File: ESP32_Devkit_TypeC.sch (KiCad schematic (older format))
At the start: 43 parts, among them J1 USB_C_Receptacle_USB2.0, J2 Conn_01x19, J3 Conn_01x19, Q1 SS8050, Q2 SS8050, SW1 EN, SW2 BOOT, U1 MP2451, U2 CH340G, U3 ESP32-PICO-D4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

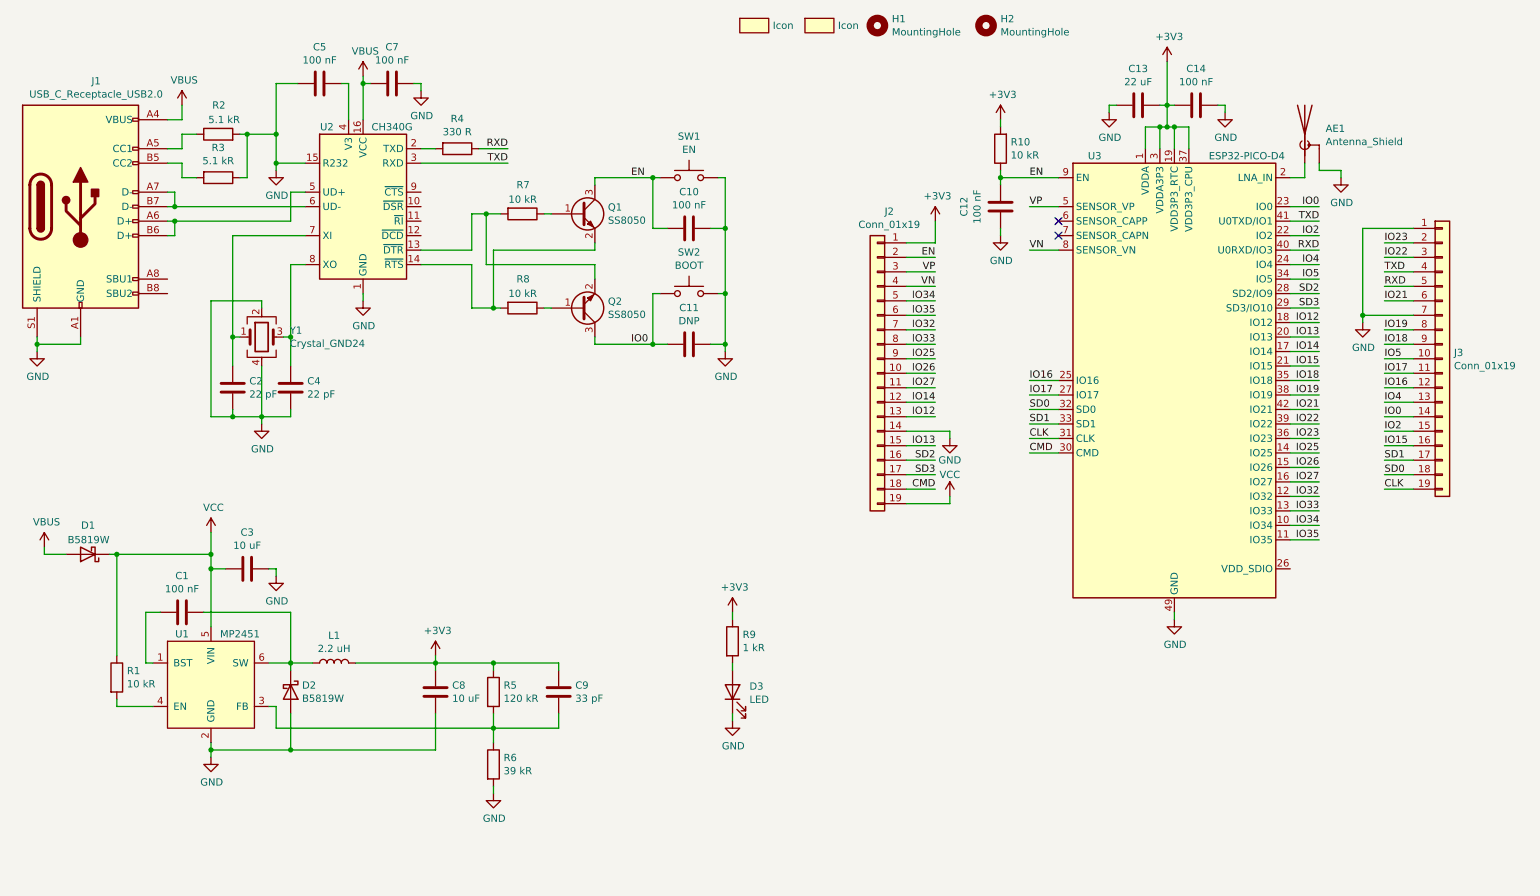
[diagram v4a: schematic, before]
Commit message: Rev B
Changes from Rev A:
 - Fix ESP32 Pico D4 footprint, now LGA
 - Add couple capacitor from EN to IO0
 - Add protection resistors to EN and IO0
 - Move VBUS diode for easier USB Type C jack assembly
 - Small routing optimizations
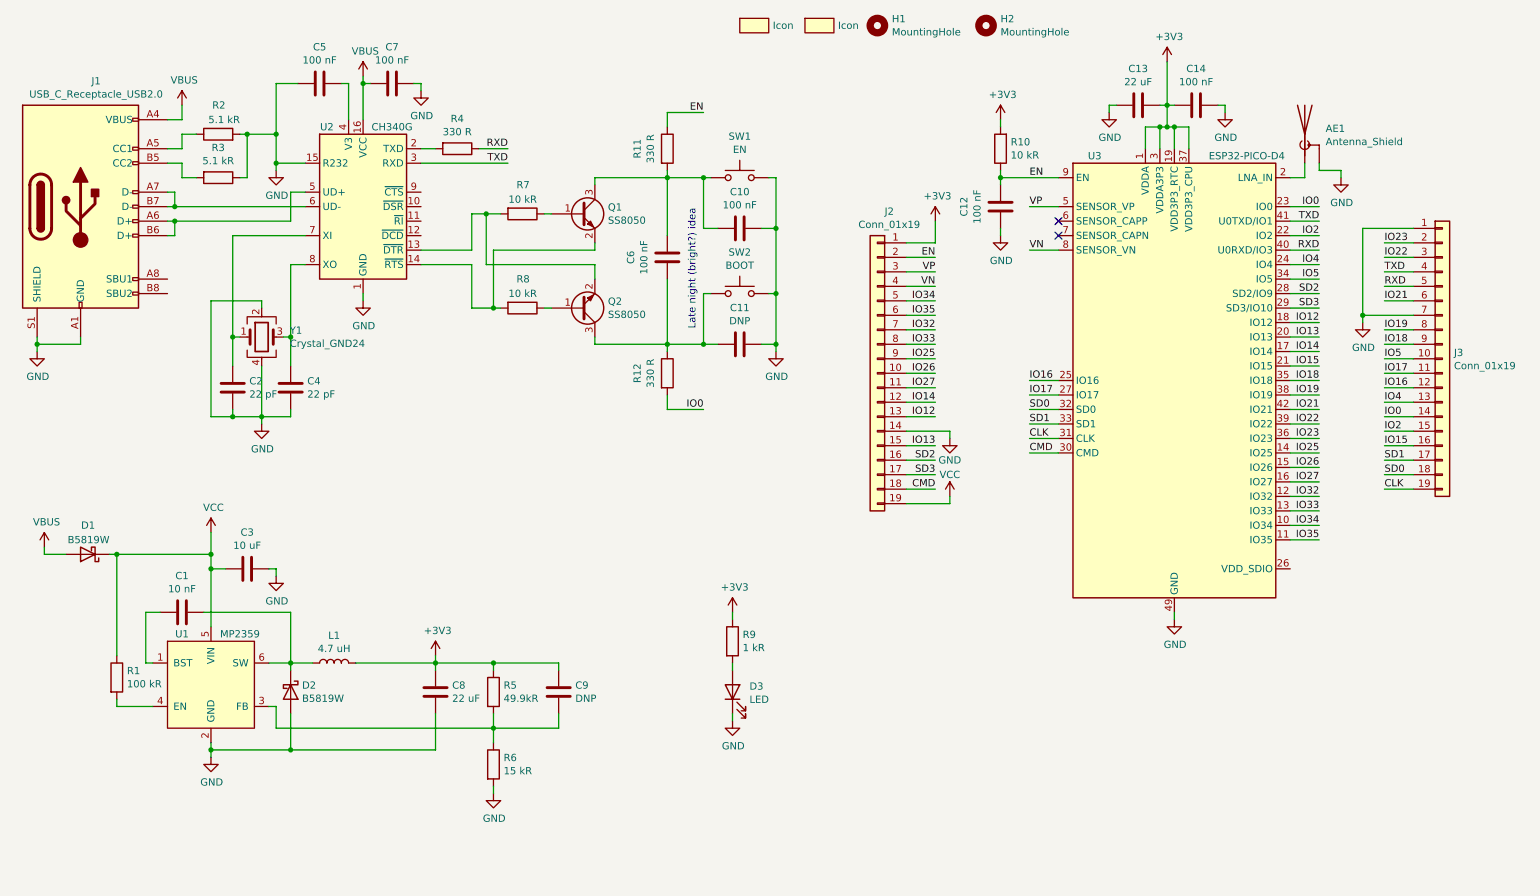
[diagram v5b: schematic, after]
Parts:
- added C6: 100 nF, Capacitor_SMD:C_0402_1005Metric, symbol Device:C
- added R11, R12: 330 R, Resistor_SMD:R_0402_1005Metric, symbol Device:R
- C1: value 100 nF -> 10 nF; LCSC C1525 -> C15195
- C8: value 10 uF -> 22 uF; LCSC C19702 -> C59461
- C9: value 33 pF -> DNP; LCSC C1562 -> (none)
- L1: value 2.2 uH -> 4.7 uH; LCSC C86074 -> C86070
- R1: value 10 kR -> 100 kR; LCSC C25744 -> C25741
- R5: value 120 kR -> 49.9kR; LCSC C25750 -> C25897
- R6: value 39 kR -> 15 kR; LCSC C25783 -> C25756
- U1: value MP2451 -> MP2359; LCSC C14123 -> C14259
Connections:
- net EN: now also R11.1; no longer C10.2, Q1.3 (C), SW1.1
- net IO0: now also R12.2; no longer C11.2, Q2.3 (C), SW2.1
- new net: C10.2, C6.1, Q1.3 (C), R11.2, SW1.1
- new net: C11.2, C6.2, Q2.3 (C), R12.1, SW2.1
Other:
- note added: "Late night (bright?) idea"
- moved on the sheet: C10, C11, SW1, SW2
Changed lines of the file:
@@
 P 2200 5150
 F 0 "U1" H 2000 5500 50  0000 C CNN
-F 1 "MP2451" H 2400 5500 50  0000 C CNN
+F 1 "MP2359" H 2400 5500 50  0000 C CNN
 F 2 "Package_TO_SOT_SMD:SOT-23-6" H 2200 6100 50  0001 C CNN
 F 3 "https://datasheet.lcsc.com/szlcsc/Monolithic-Power-Systems-MPS-MP2451DT-LF-Z_C14123.pdf" H 2200 6100 50  0001 C CNN
-F 4 "C14123" H 2200 5150 50  0001 C CNN "LCSC"
+F 4 "C14259" H 2200 5150 50  0001 C CNN "LCSC"
 	1    2200 5150
 	1    0    0    -1
@@
 P 3050 5000
 F 0 "L1" V 3240 5000 50  0000 C CNN
-F 1 "2.2 uH" V 3149 5000 50  0000 C CNN
+F 1 "4.7 uH" V 3149 5000 50  0000 C CNN
 F 2 "Inductor_SMD:L_1210_3225Metric" H 3050 5000 50  0001 C CNN
 F 3 "~" H 3050 5000 50  0001 C CNN
-F 4 "C86074" V 3050 5000 50  0001 C CNN "LCSC"
+F 4 "C86070" V 3050 5000 50  0001 C CNN "LCSC"
 	1    3050 5000
 	0    -1   -1   0
@@
 P 3750 5200
 F 0 "C8" H 3865 5246 50  0000 L CNN
-F 1 "10 uF" H 3865 5155 50  0000 L CNN
+F 1 "22 uF" H 3865 5155 50  0000 L CNN
 F 2 "Capacitor_SMD:C_0603_1608Metric" H 3788 5050 50  0001 C CNN
 F 3 "~" H 3750 5200 50  0001 C CNN
-F 4 "C19702" H 3750 5200 50  0001 C CNN "LCSC"
+F 4 "C59461" H 3750 5200 50  0001 C CNN "LCSC"
 	1    3750 5200
 	1    0    0    -1
@@
 P 4150 5200
 F 0 "R5" H 4220 5246 50  0000 L CNN
-F 1 "120 kR" H 4220 5155 50  0000 L CNN
+F 1 "49.9kR" H 4220 5155 50  0000 L CNN
 F 2 "Resistor_SMD:R_0402_1005Metric" V 4080 5200 50  0001 C CNN
 F 3 "~" H 4150 5200 50  0001 C CNN
-F 4 "C25750" H 4150 5200 50  0001 C CNN "LCSC"
+F 4 "C25897" H 4150 5200 50  0001 C CNN "LCSC"
 	1    4150 5200
 	1    0    0    -1
@@
 P 4150 5700
 F 0 "R6" H 4220 5746 50  0000 L CNN
-F 1 "39 kR" H 4220 5655 50  0000 L CNN
+F 1 "15 kR" H 4220 5655 50  0000 L CNN
 F 2 "Resistor_SMD:R_0402_1005Metric" V 4080 5700 50  0001 C CNN
 F 3 "~" H 4150 5700 50  0001 C CNN
-F 4 "C25783" H 4150 5700 50  0001 C CNN "LCSC"
+F 4 "C25756" H 4150 5700 50  0001 C CNN "LCSC"
 	1    4150 5700
 	1    0    0    -1
@@
 P 4600 5200
 F 0 "C9" H 4715 5246 50  0000 L CNN
-F 1 "33 pF" H 4715 5155 50  0000 L CNN
+F 1 "DNP" H 4715 5155 50  0000 L CNN
 F 2 "Capacitor_SMD:C_0402_1005Metric" H 4638 5050 50  0001 C CNN
 F 3 "" H 4600 5200 50  0001 C CNN
-F 4 "C1562" H 4600 5200 50  0001 C CNN "LCSC"
 	1    4600 5200
 	1    0    0    -1
@@
 P 2000 4650
 F 0 "C1" V 1748 4650 50  0000 C CNN
-F 1 "100 nF" V 1839 4650 50  0000 C CNN
+F 1 "10 nF" V 1839 4650 50  0000 C CNN
 F 2 "Capacitor_SMD:C_0402_1005Metric" H 2038 4500 50  0001 C CNN
 F 3 "~" H 2000 4650 50  0001 C CNN
-F 4 "C1525" H 2000 4650 50  0001 C CNN "LCSC"
+F 4 "C15195" H 2000 4650 50  0001 C CNN "LCSC"
 	1    2000 4650
 	0    1    1    0
@@
 P 1550 5100
 F 0 "R1" H 1620 5146 50  0000 L CNN
-F 1 "10 kR" H 1620 5055 50  0000 L CNN
+F 1 "100 kR" H 1620 5055 50  0000 L CNN
 F 2 "Resistor_SMD:R_0402_1005Metric" V 1480 5100 50  0001 C CNN
 F 3 "~" H 1550 5100 50  0001 C CNN
-F 4 "C25744" H 1550 5100 50  0001 C CNN "LCSC"
+F 4 "C25741" H 1550 5100 50  0001 C CNN "LCSC"
 	1    1550 5100
 	1    0    0    -1
@@
 L Switch:SW_Push SW1
 U 1 1 5ECA28F9
-P 5500 1650
-F 0 "SW1" H 5500 1935 50  0000 C CNN
-F 1 "EN" H 5500 1844 50  0000 C CNN
-F 2 "Button_Switch_SMD:SW_Push_SPST_NO_Alps_SKRK" H 5500 1850 50  0001 C CNN
-F 3 "~" H 5500 1850 50  0001 C CNN
-F 4 "C115357" H 5500 1650 50  0001 C CNN "LCSC"
-	1    5500 1650
+P 5850 1650
+F 0 "SW1" H 5850 1935 50  0000 C CNN
+F 1 "EN" H 5850 1844 50  0000 C CNN
+F 2 "Button_Switch_SMD:SW_Push_SPST_NO_Alps_SKRK" H 5850 1850 50  0001 C CNN
+F 3 "~" H 5850 1850 50  0001 C CNN
+F 4 "C115357" H 5850 1650 50  0001 C CNN "LCSC"
+	1    5850 1650
 	1    0    0    -1
 $EndComp
@@
 L Switch:SW_Push SW2
 U 1 1 5ECA6673
-P 5500 2450
-F 0 "SW2" H 5500 2735 50  0000 C CNN
-F 1 "BOOT" H 5500 2644 50  0000 C CNN
-F 2 "Button_Switch_SMD:SW_Push_SPST_NO_Alps_SKRK" H 5500 2650 50  0001 C CNN
-F 3 "~" H 5500 2650 50  0001 C CNN
-F 4 "C115357" H 5500 2450 50  0001 C CNN "LCSC"
-	1    5500 2450
+P 5850 2450
+F 0 "SW2" H 5850 2735 50  0000 C CNN
+F 1 "BOOT" H 5850 2644 50  0000 C CNN
+F 2 "Button_Switch_SMD:SW_Push_SPST_NO_Alps_SKRK" H 5850 2650 50  0001 C CNN
+F 3 "~" H 5850 2650 50  0001 C CNN
+F 4 "C115357" H 5850 2450 50  0001 C CNN "LCSC"
+	1    5850 2450
 	1    0    0    -1
 $EndComp
@@
 L Device:C C11
 U 1 1 5EF0984E
-P 5500 2800
-F 0 "C11" V 5248 2800 50  0000 C CNN
-F 1 "DNP" V 5339 2800 50  0000 C CNN
-F 2 "Capacitor_SMD:C_0402_1005Metric" H 5538 2650 50  0001 C CNN
-F 3 "~" H 5500 2800 50  0001 C CNN
-	1    5500 2800
+P 5850 2800
+F 0 "C11" V 5598 2800 50  0000 C CNN
+F 1 "DNP" V 5689 2800 50  0000 C CNN
+F 2 "Capacitor_SMD:C_0402_1005Metric" H 5888 2650 50  0001 C CNN
+F 3 "~" H 5850 2800 50  0001 C CNN
+	1    5850 2800
 	0    1    1    0
 $EndComp
@@
 L Device:C C10
 U 1 1 5EF13A64
-P 5500 2000
-F 0 "C10" V 5248 2000 50  0000 C CNN
-F 1 "100 nF" V 5339 2000 50  0000 C CNN
-F 2 "Capacitor_SMD:C_0402_1005Metric" H 5538 1850 50  0001 C CNN
-F 3 "~" H 5500 2000 50  0001 C CNN
-F 4 "C1525" H 5500 2000 50  0001 C CNN "LCSC"
-	1    5500 2000
+P 5850 2000
+F 0 "C10" V 5598 2000 50  0000 C CNN
+F 1 "100 nF" V 5689 2000 50  0000 C CNN
+F 2 "Capacitor_SMD:C_0402_1005Metric" H 5888 1850 50  0001 C CNN
+F 3 "~" H 5850 2000 50  0001 C CNN
+F 4 "C1525" H 5850 2000 50  0001 C CNN "LCSC"
+	1    5850 2000
 	0    1    1    0
 $EndComp
 Wire Wire Line
-	5700 2450 5750 2450
-Wire Wire Line
-	5750 2450 5750 2800
-Wire Wire Line
-	5750 2800 5650 2800
-Wire Wire Line
-	5350 2800 5250 2800
-Wire Wire Line
-	5250 2800 5250 2450
-Wire Wire Line
-	5250 2450 5300 2450
-Wire Wire Line
-	5300 1650 5250 1650
-Wire Wire Line
-	5250 1650 5250 2000
-Wire Wire Line
-	5250 2000 5350 2000
-Wire Wire Line
-	5700 1650 5750 1650
-Wire Wire Line
-	5750 1650 5750 2000
-Wire Wire Line
-	5650 2000 5750 2000
+	6050 2450 6100 2450
+Wire Wire Line
+	6100 2450 6100 2800
+Wire Wire Line
+	6100 2800 6000 2800
+Wire Wire Line
+	5700 2800 5600 2800
+Wire Wire Line
+	5600 2800 5600 2450
+Wire Wire Line
+	5600 2450 5650 2450
+Wire Wire Line
+	5650 1650 5600 1650
+Wire Wire Line
+	5600 1650 5600 2000
+Wire Wire Line
+	5600 2000 5700 2000
+Wire Wire Line
+	6050 1650 6100 1650
+Wire Wire Line
+	6100 1650 6100 2000
+Wire Wire Line
+	6000 2000 6100 2000
 $Comp
 L Device:C C12
@@
 L power:GND #PWR0123
 U 1 1 5F0F7667
-P 5750 2850
-F 0 "#PWR0123" H 5750 2600 50  0001 C CNN
-F 1 "GND" H 5755 2677 50  0000 C CNN
-F 2 "" H 5750 2850 50  0001 C CNN
-F 3 "" H 5750 2850 50  0001 C CNN
-	1    5750 2850
-	1    0    0    -1
-$EndComp
-Wire Wire Line
-	5750 2850 5750 2800
-Connection ~ 5750 2800
-Wire Wire Line
-	5750 2450 5750 2000
-Connection ~ 5750 2450
-Connection ~ 5750 2000
-Text Label 5100 1650 0    50   ~ 0
+P 6100 2850
+F 0 "#PWR0123" H 6100 2600 50  0001 C CNN
+F 1 "GND" H 6105 2677 50  0000 C CNN
+F 2 "" H 6100 2850 50  0001 C CNN
+F 3 "" H 6100 2850 50  0001 C CNN
+	1    6100 2850
+	1    0    0    -1
+$EndComp
+Wire Wire Line
+	6100 2850 6100 2800
+Connection ~ 6100 2800
+Wire Wire Line
+	6100 2450 6100 2000
+Connection ~ 6100 2450
+Connection ~ 6100 2000
+Text Label 5600 1200 2    50   ~ 0
 EN
-Text Label 5100 2800 0    50   ~ 0
+Text Label 5600 3250 2    50   ~ 0
 IO0
 $Comp
@@
 	1    0    0    -1
 $EndComp
-Connection ~ 5250 1650
-Connection ~ 5250 2800
-Wire Wire Line
-	4850 1650 5250 1650
-Wire Wire Line
-	4850 2800 5250 2800
+Connection ~ 5600 1650
+Connection ~ 5600 2800
+$Comp
+L Device:C C6
+U 1 1 5ECF6C76
+P 5350 2200
+F 0 "C6" V 5098 2200 50  0000 C CNN
+F 1 "100 nF" V 5189 2200 50  0000 C CNN
+F 2 "Capacitor_SMD:C_0402_1005Metric" H 5388 2050 50  0001 C CNN
+F 3 "~" H 5350 2200 50  0001 C CNN
+F 4 "C1525" H 5350 2200 50  0001 C CNN "LCSC"
+	1    5350 2200
+	1    0    0    -1
+$EndComp
+Wire Wire Line
+	5350 2050 5350 1650
+Connection ~ 5350 1650
+Wire Wire Line
+	5350 1650 5600 1650
+Wire Wire Line
+	4850 1650 5350 1650
+Wire Wire Line
+	4850 2800 5350 2800
+Wire Wire Line
+	5350 2350 5350 2800
+Connection ~ 5350 2800
+Wire Wire Line
+	5350 2800 5600 2800
+Text Notes 5550 2700 1    50   ~ 0
+Late night (bright?) idea
+$Comp
+L Device:R R11
+U 1 1 5ED69DE0
+P 5350 1450
+F 0 "R11" V 5143 1450 50  0000 C CNN
+F 1 "330 R" V 5234 1450 50  0000 C CNN
+F 2 "Resistor_SMD:R_0402_1005Metric" V 5280 1450 50  0001 C CNN
+F 3 "~" H 5350 1450 50  0001 C CNN
+F 4 "C25104" V 5350 1450 50  0001 C CNN "LCSC"
+	1    5350 1450
+	1    0    0    -1
+$EndComp
+Wire Wire Line
+	5350 1650 5350 1600
+Wire Wire Line
+	5350 1300 5350 1200
+Wire Wire Line
+	5350 1200 5600 1200
+$Comp
+L Device:R R12
+U 1 1 5ED98EF5
+P 5350 3000
+F 0 "R12" V 5143 3000 50  0000 C CNN
+F 1 "330 R" V 5234 3000 50  0000 C CNN
+F 2 "Resistor_SMD:R_0402_1005Metric" V 5280 3000 50  0001 C CNN
+F 3 "~" H 5350 3000 50  0001 C CNN
+F 4 "C25104" V 5350 3000 50  0001 C CNN "LCSC"
+	1    5350 3000
+	1    0    0    -1
+$EndComp
+Wire Wire Line
+	5350 2850 5350 2800
+Wire Wire Line
+	5350 3250 5600 3250
+Wire Wire Line
+	5350 3150 5350 3250
 $EndSCHEMATC

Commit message: Rev C
Changes from Rev B:

* Add more bypassing to ESP32 Pico D4
* Reduce ground loop area of step-down significantly
* Fix ugly routing of USB D+
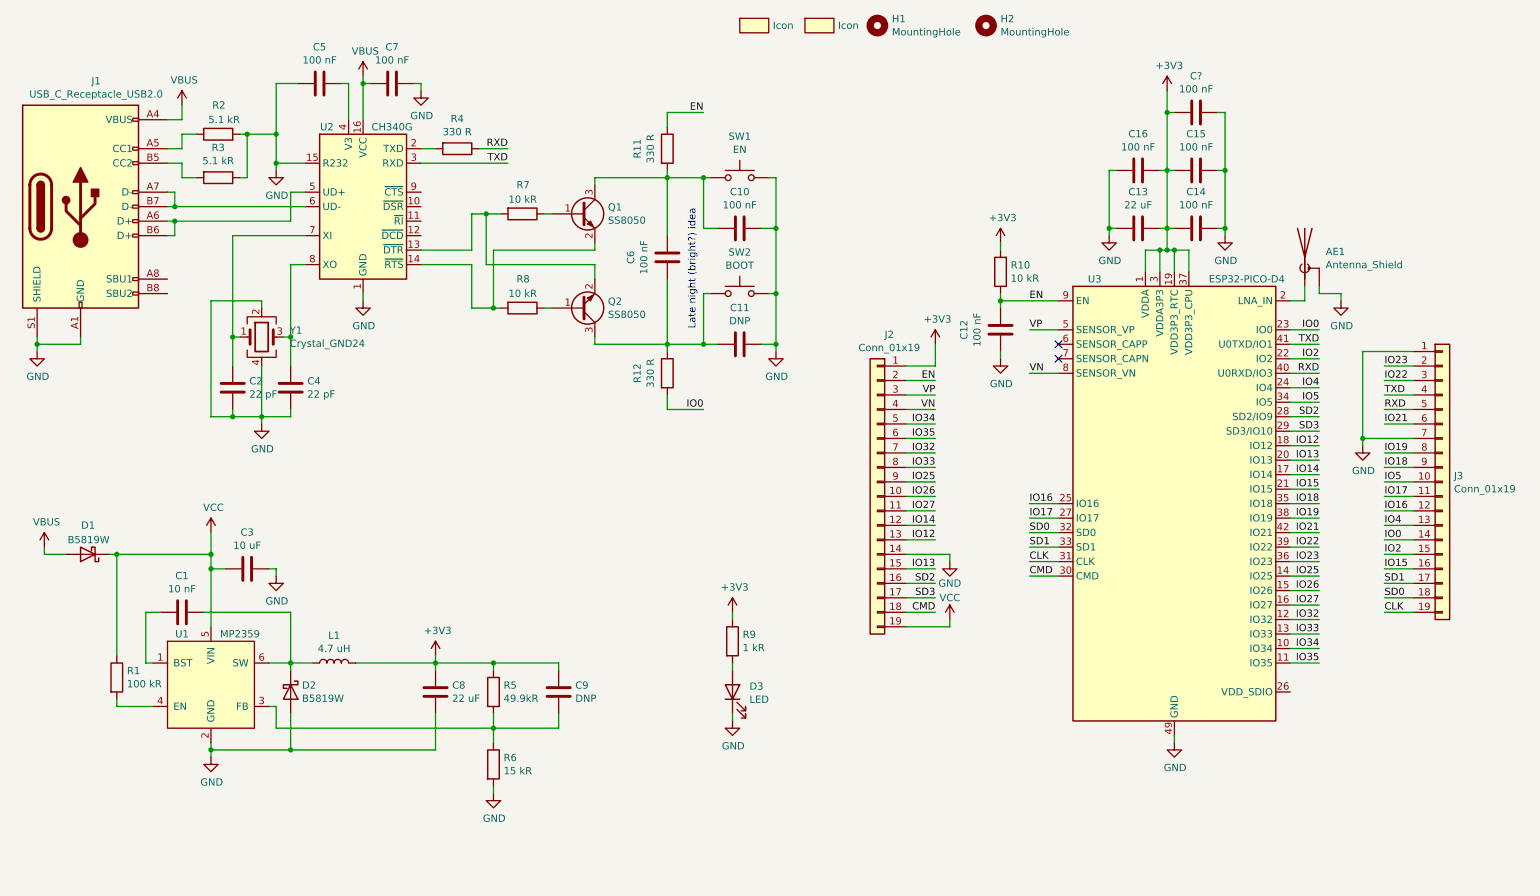
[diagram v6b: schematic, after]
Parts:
- added C15, C16, C?: 100 nF, Capacitor_SMD:C_0402_1005Metric, symbol Device:C
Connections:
- net +3V3: now also C15.2, C16.1, C?.2
- net GND: now also C15.1, C16.2, C?.1
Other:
- moved on the sheet: AE1, C12, C13, C14, J2, J3, R10, U3
